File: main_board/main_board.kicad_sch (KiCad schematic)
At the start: 15 parts, among them J1 CON-SMA-EDGE-S, J2 TSW-104-14-F-S, J3 TSW-104-14-F-S, U2 TS5A4624DCKR, U4 TS5A4624DCKR

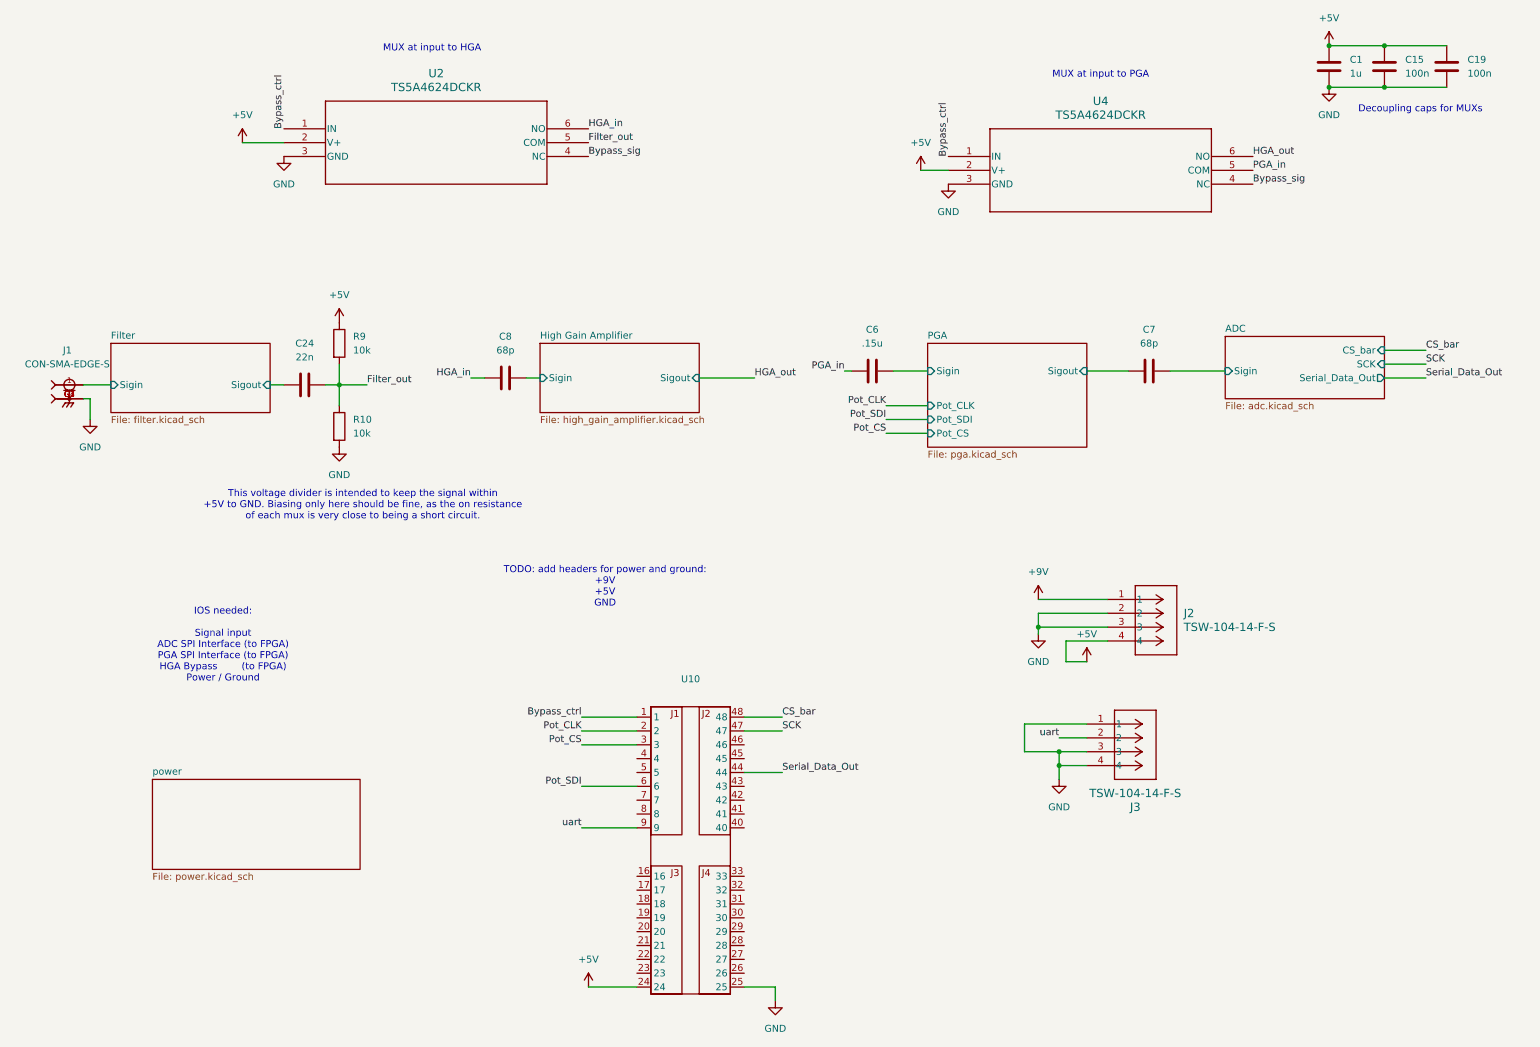
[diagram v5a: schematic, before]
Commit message: Final Schematic is frozen, DO NOT MAKE CHANGES WITHOUT GROUP AGREEMENT. Also floorplan all major ICs on board.
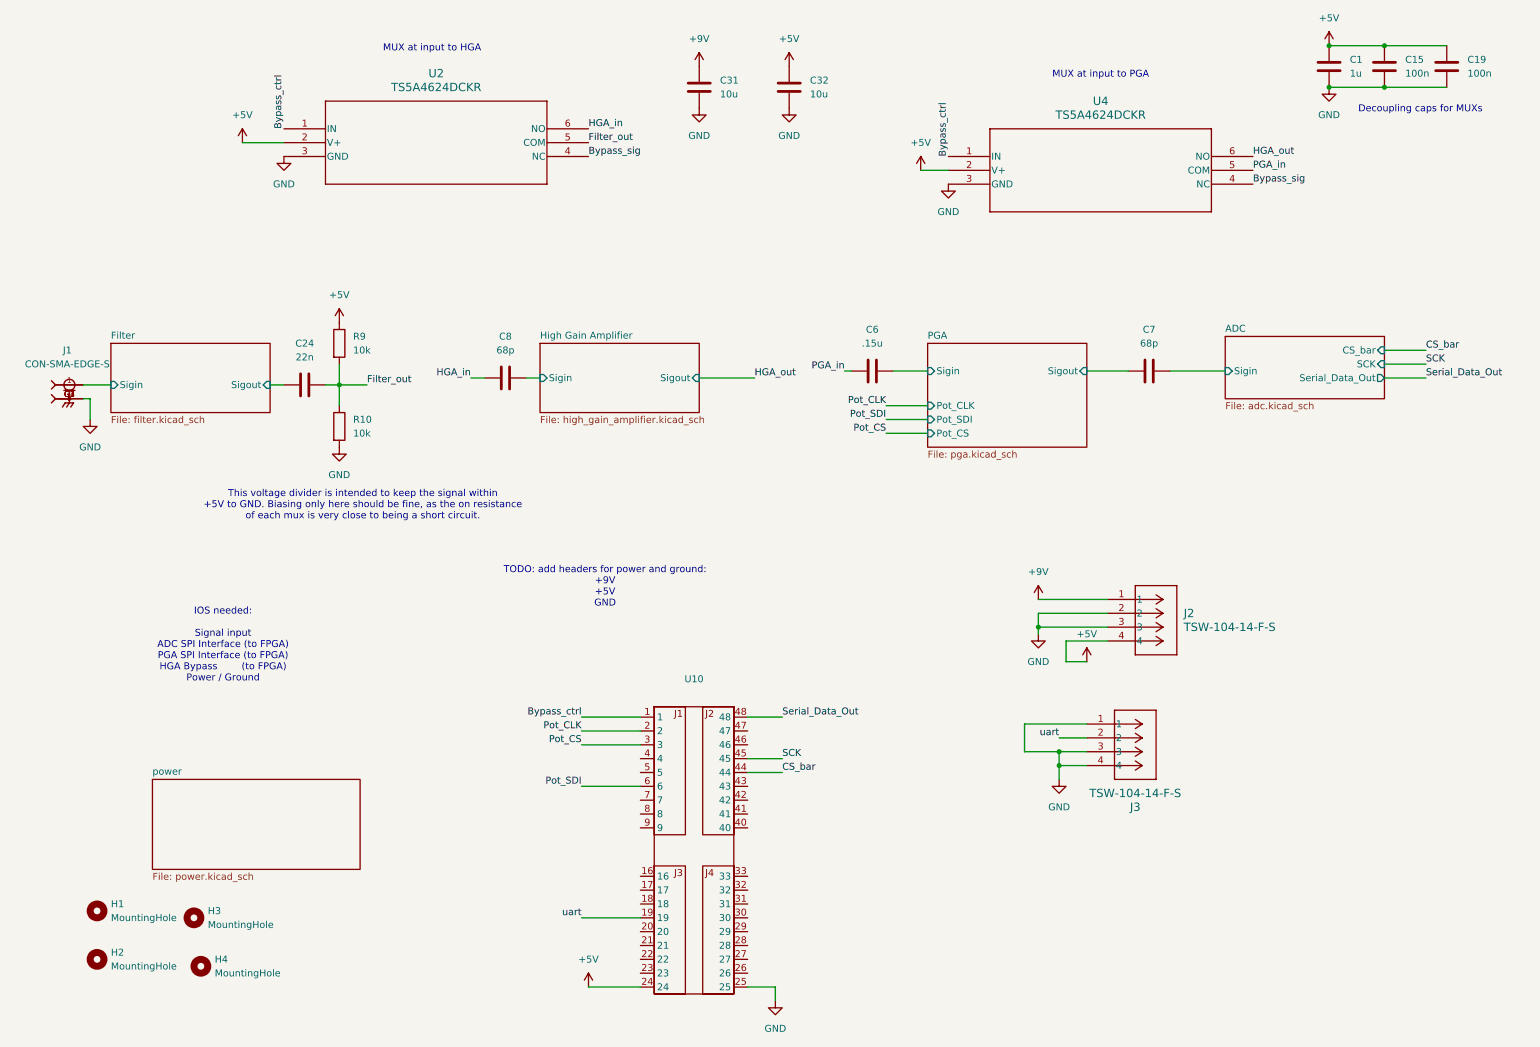
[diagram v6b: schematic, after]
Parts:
- added C31, C32: 10u, Capacitor_SMD:C_0603_1608Metric, symbol Device:C
- added H1, H2, H3, H4: MountingHole, MountingHole:MountingHole_2mm, symbol Mechanical:MountingHole
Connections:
- net +5V: now also C32.1
- net +9V: now also C31.1
- net CS_bar: now also U10.44; no longer U10.48
- net GND: now also C31.2, C32.2
- net SCK: now also U10.45; no longer U10.47
- net Serial_Data_Out: now also U10.48; no longer U10.44
- net uart: now also U10.19; no longer U10.9
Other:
- moved on the sheet: U10

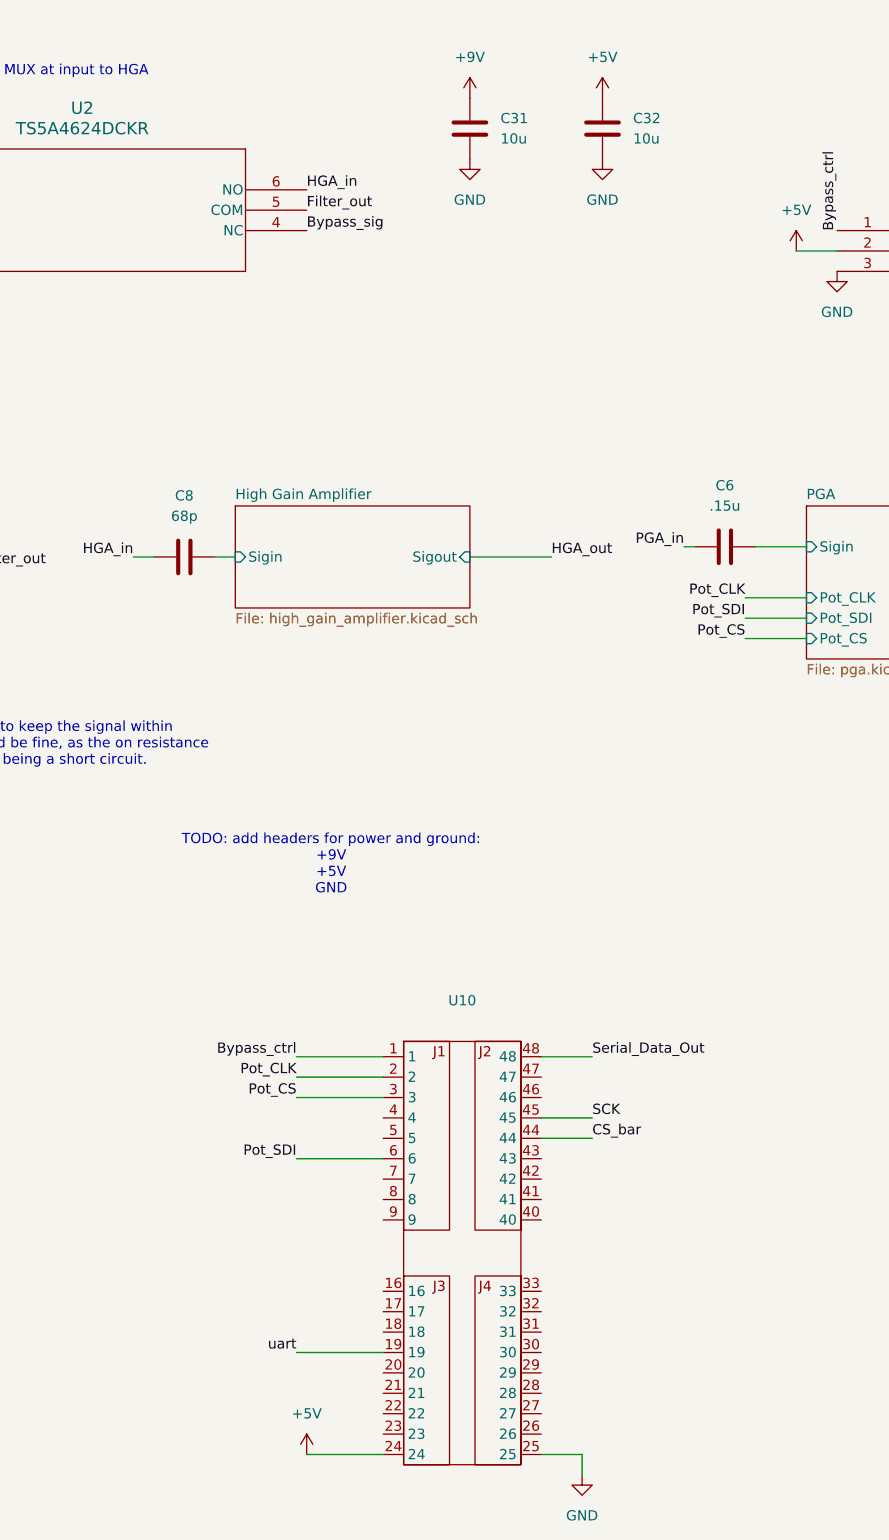
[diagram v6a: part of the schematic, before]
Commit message: Layout hase been floorplaned, needs routing.
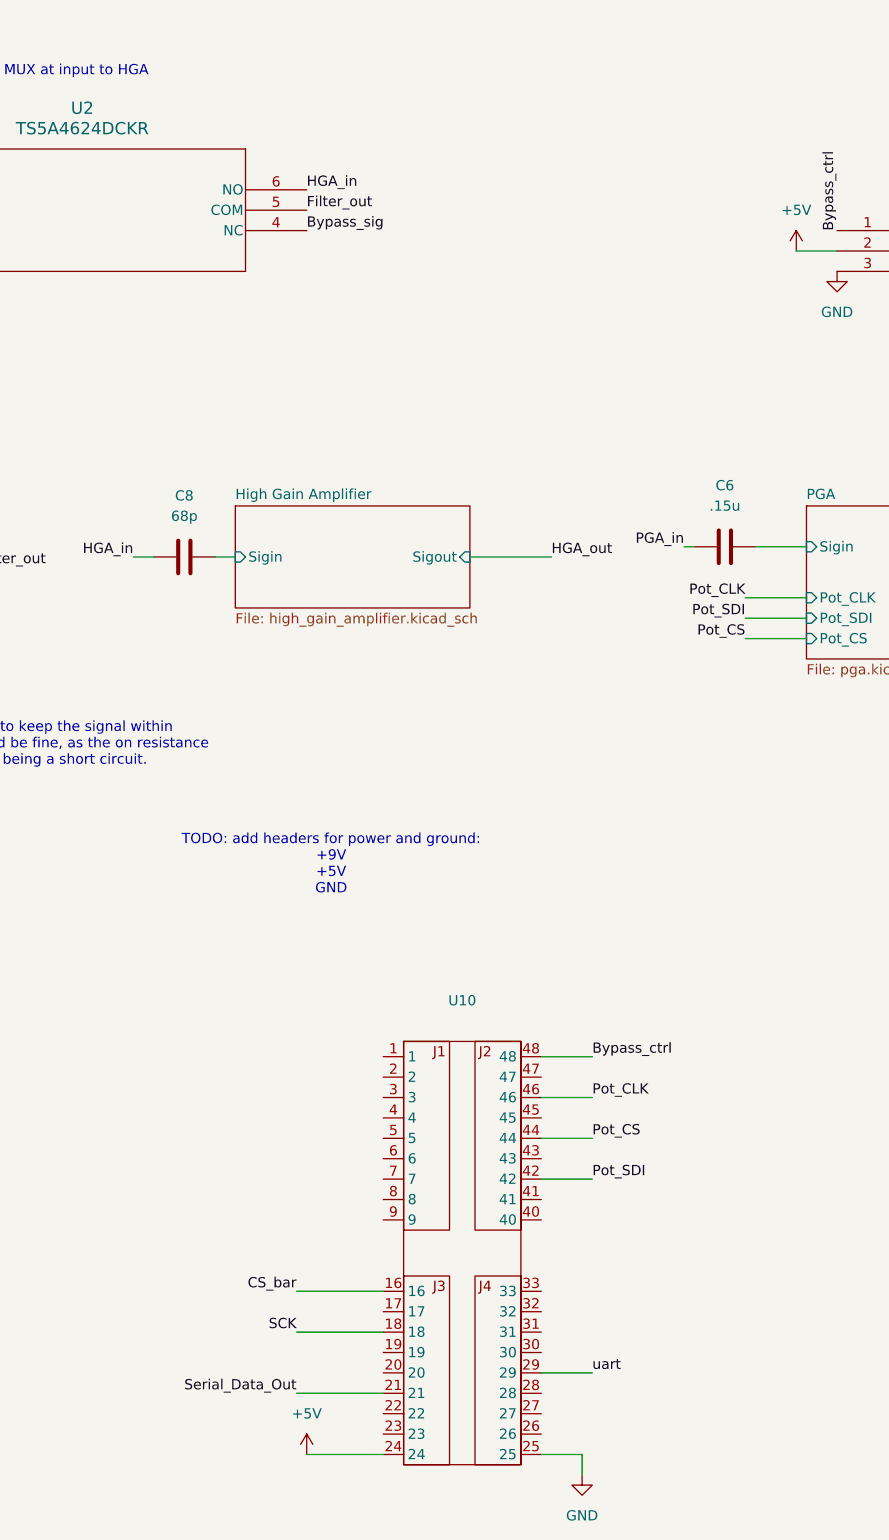
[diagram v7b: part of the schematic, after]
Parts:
- removed C31, C32: 10u, Capacitor_SMD:C_0603_1608Metric, symbol Device:C
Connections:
- net Bypass_ctrl: now also U10.48; no longer U10.1
- net CS_bar: now also U10.16; no longer U10.44
- net Pot_CLK: now also U10.46; no longer U10.2
- net Pot_CS: now also U10.44; no longer U10.3
- net Pot_SDI: now also U10.42; no longer U10.6
- net SCK: now also U10.18; no longer U10.45
- net Serial_Data_Out: now also U10.21; no longer U10.48
- net uart: now also U10.29; no longer U10.19

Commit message: finished board, waiting for approval.
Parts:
- added C31, C32: 10u, symbol Device:C
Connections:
- net +5V: now also C32.1
- net +9V: now also C31.1
- net GND: now also C31.2, C32.2
- net Serial_Data_Out: now also U10.20; no longer U10.21
